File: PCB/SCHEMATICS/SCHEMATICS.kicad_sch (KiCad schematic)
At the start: 0 parts

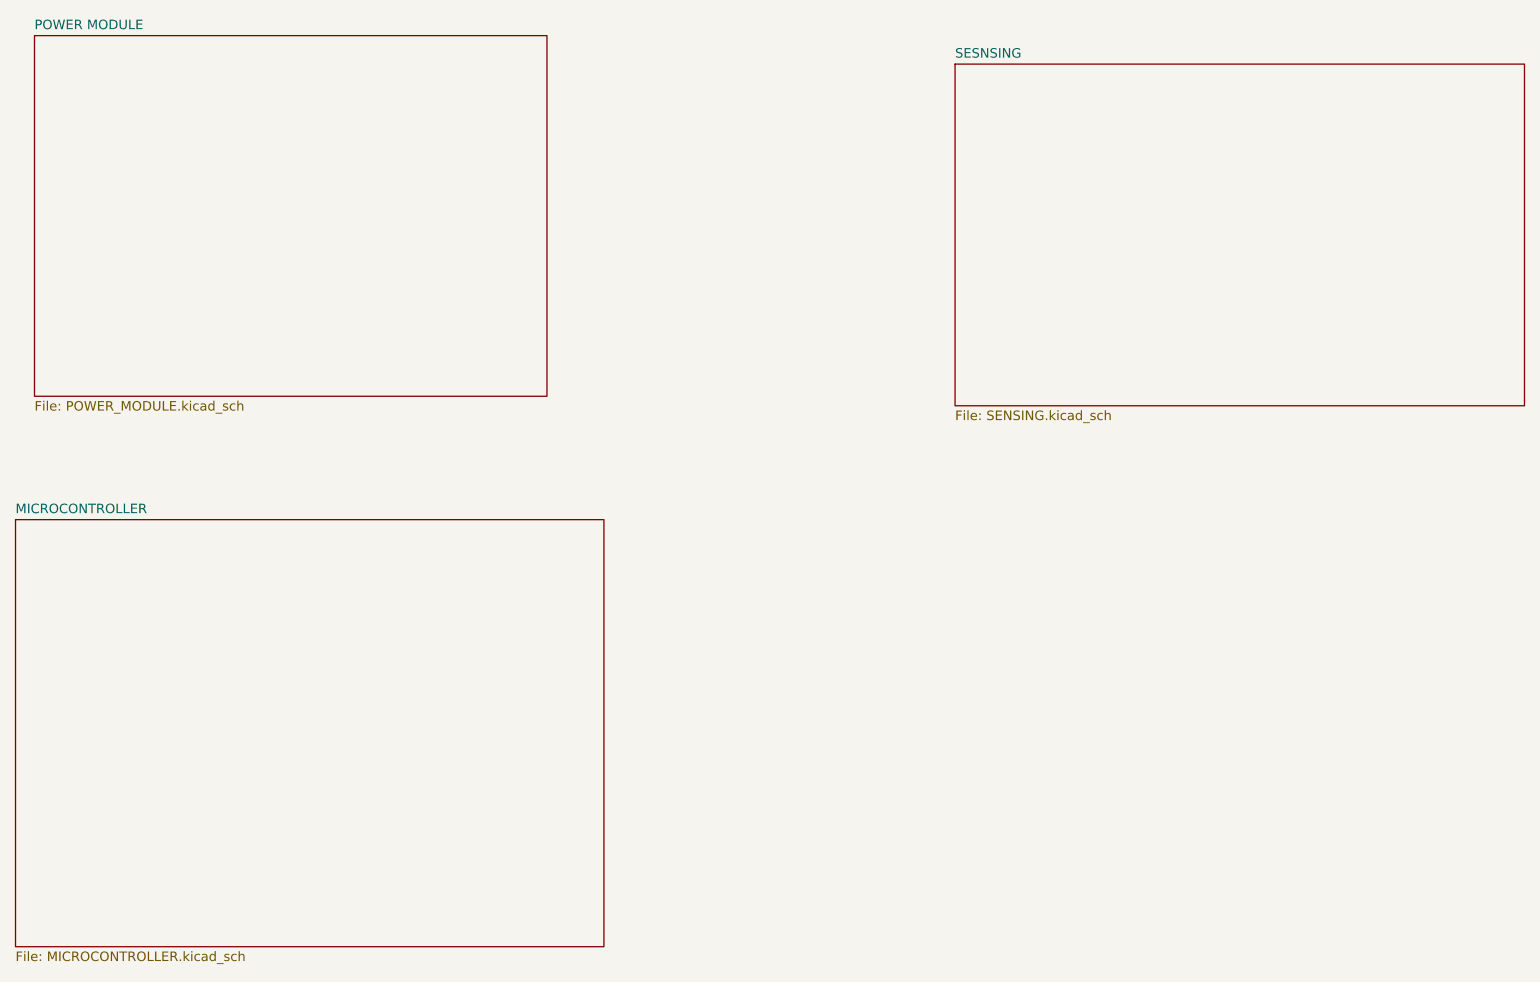
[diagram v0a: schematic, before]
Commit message: Fixed ercs
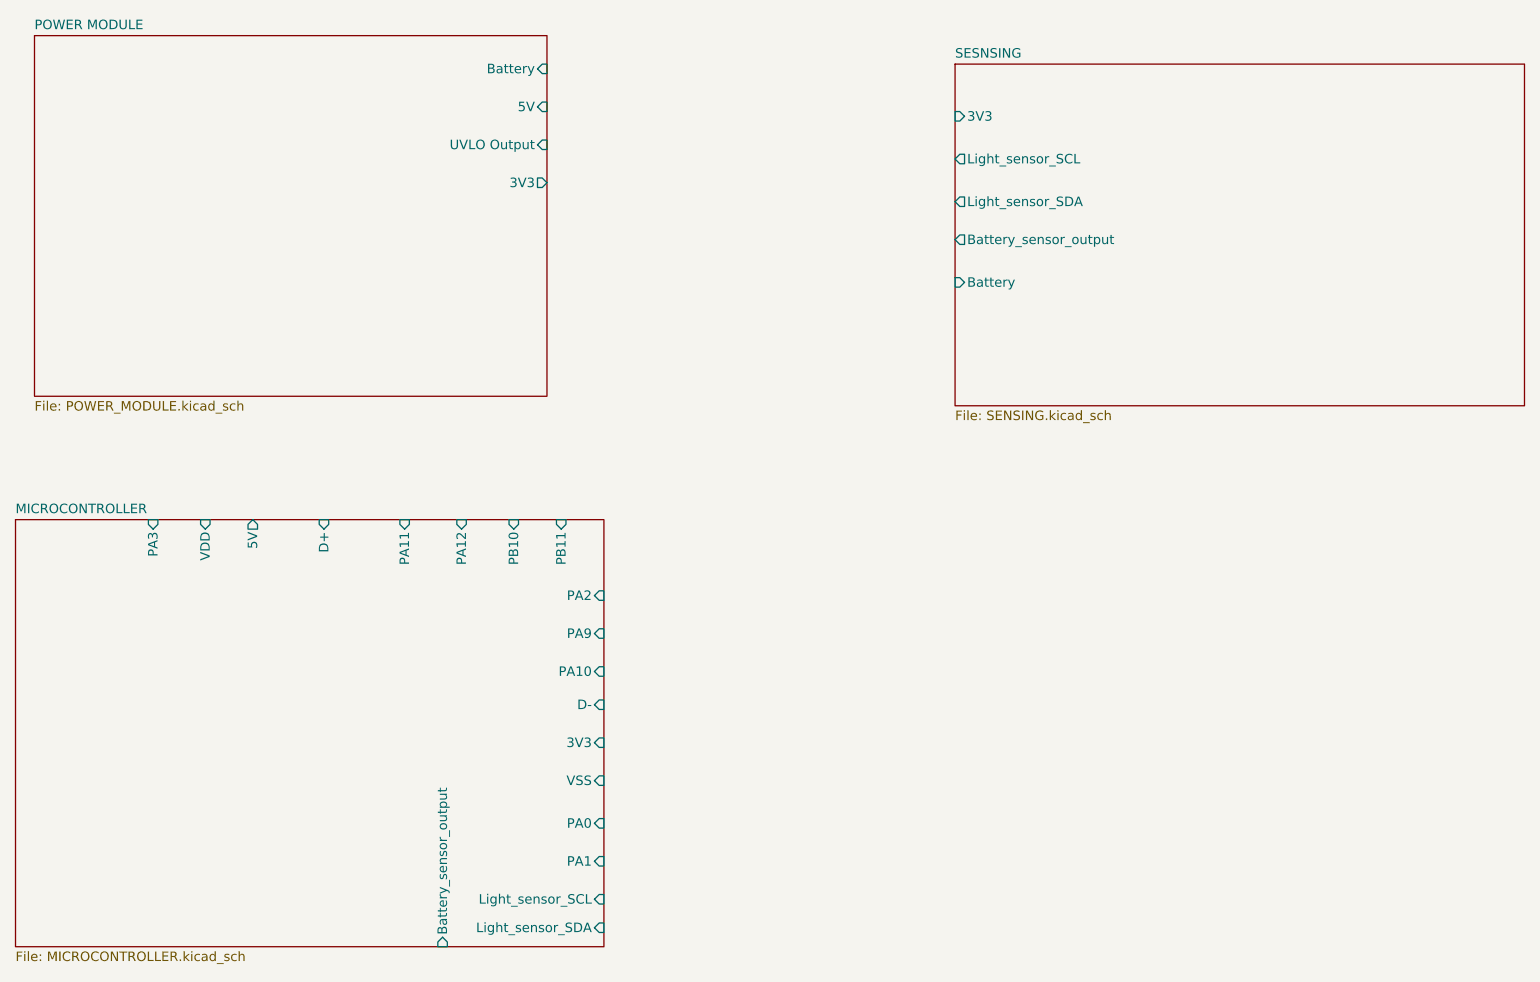
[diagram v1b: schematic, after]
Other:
- sheet MICROCONTROLLER ports: added 3V3, 5V, Battery_sensor_output, D+, D-, Light_sensor_SCL, Light_sensor_SDA, PA0, PA1, PA10, PA11, PA12, PA2, PA3, PA9, PB10, PB11, VDD, VSS; removed none
- sheet POWER MODULE ports: added 3V3, 5V, Battery, UVLO Output; removed none
- sheet SESNSING ports: added 3V3, Battery, Battery_sensor_output, Light_sensor_SCL, Light_sensor_SDA; removed none
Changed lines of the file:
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@@
       (effects (font (size 1.27 1.27)) (justify left top))
+    )
+    (pin "3V3" input (at 171.45 46.355 180)
+      (effects (font (size 1.27 1.27)) (justify left))
+    )
+    (pin "Light_sensor_SCL" output (at 171.45 52.07 180)
+      (effects (font (size 1.27 1.27)) (justify left))
+    )
+    (pin "Light_sensor_SDA" output (at 171.45 57.785 180)
+      (effects (font (size 1.27 1.27)) (justify left))
+    )
+    (pin "Battery_sensor_output" output (at 171.45 62.865 180)
+      (effects (font (size 1.27 1.27)) (justify left))
+    )
+    (pin "Battery" input (at 171.45 68.58 180)
+      (effects (font (size 1.27 1.27)) (justify left))
     )
     (instances
@@
       (effects (font (size 1.27 1.27)) (justify left top))
     )
+    (pin "Battery" input (at 116.84 40.005 0)
+      (effects (font (size 1.27 1.27)) (justify right))
+    )
+    (pin "5V" input (at 116.84 45.085 0)
+      (effects (font (size 1.27 1.27)) (justify right))
+    )
+    (pin "UVLO Output" input (at 116.84 50.165 0)
+      (effects (font (size 1.27 1.27)) (justify right))
+    )
+    (pin "3V3" output (at 116.84 55.245 0)
+      (effects (font (size 1.27 1.27)) (justify right))
+    )
     (instances
       (project "SCHEMATICS"
@@
       (effects (font (size 1.27 1.27)) (justify left top))
     )
+    (pin "D+" input (at 86.995 100.33 90)
+      (effects (font (size 1.27 1.27)) (justify right))
+    )
+    (pin "PA11" input (at 97.79 100.33 90)
+      (effects (font (size 1.27 1.27)) (justify right))
+    )
+    (pin "PA12" input (at 105.41 100.33 90)
+      (effects (font (size 1.27 1.27)) (justify right))
+    )
+    (pin "PB10" input (at 112.395 100.33 90)
+      (effects (font (size 1.27 1.27)) (justify right))
+    )
+    (pin "PB11" input (at 118.745 100.33 90)
+      (effects (font (size 1.27 1.27)) (justify right))
+    )
+    (pin "5V" output (at 77.47 100.33 90)
+      (effects (font (size 1.27 1.27)) (justify right))
+    )
+    (pin "VDD" input (at 71.12 100.33 90)
+      (effects (font (size 1.27 1.27)) (justify right))
+    )
+    (pin "PA3" input (at 64.135 100.33 90)
+      (effects (font (size 1.27 1.27)) (justify right))
+    )
+    (pin "PA2" input (at 124.46 110.49 0)
+      (effects (font (size 1.27 1.27)) (justify right))
+    )
+    (pin "PA9" input (at 124.46 115.57 0)
+      (effects (font (size 1.27 1.27)) (justify right))
+    )
+    (pin "PA10" input (at 124.46 120.65 0)
+      (effects (font (size 1.27 1.27)) (justify right))
+    )
+    (pin "D-" input (at 124.46 125.095 0)
+      (effects (font (size 1.27 1.27)) (justify right))
+    )
+    (pin "3V3" input (at 124.46 130.175 0)
+      (effects (font (size 1.27 1.27)) (justify right))
+    )
+    (pin "VSS" input (at 124.46 135.255 0)
+      (effects (font (size 1.27 1.27)) (justify right))
+    )
+    (pin "PA0" input (at 124.46 140.97 0)
+      (effects (font (size 1.27 1.27)) (justify right))
+    )
+    (pin "PA1" input (at 124.46 146.05 0)
+      (effects (font (size 1.27 1.27)) (justify right))
+    )
+    (pin "Light_sensor_SCL" input (at 124.46 151.13 0)
+      (effects (font (size 1.27 1.27)) (justify right))
+    )
+    (pin "Light_sensor_SDA" input (at 124.46 154.94 0)
+      (effects (font (size 1.27 1.27)) (justify right))
+    )
+    (pin "Battery_sensor_output" input (at 102.87 157.48 270)
+      (effects (font (size 1.27 1.27)) (justify left))
+    )
     (instances

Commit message: Fixing ERCs
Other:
- sheet MICROCONTROLLER ports: added none; removed D+, D-, PA0, PA1, PA10, PA11, PA12, PA2, PA3, PA9, PB10, PB11, VDD, VSS
- sheet POWER MODULE ports: added none; removed UVLO Output
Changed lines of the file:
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@@
 (kicad_sch (version 20230121) (generator eeschema)
   (paper "A4")
-  (sheet (at 171.45 39.37) (size 76.2 45.72) (fields_autoplaced)
+  (junction (at 121.92 42.545) (diameter 0) (color 0 0 0 0)
+  )
+  (wire (pts (xy 146.05 114.935) (xy 146.05 54.61))
+    (stroke (width 0) (type default))
+  )
+  (wire (pts (xy 144.78 111.125) (xy 144.78 48.895))
+    (stroke (width 0) (type default))
+  )
+  (wire (pts (xy 124.46 111.125) (xy 144.78 111.125))
+    (stroke (width 0) (type default))
+  )
+  (wire (pts (xy 121.92 42.545) (xy 170.18 42.545))
+    (stroke (width 0) (type default))
+  )
+  (wire (pts (xy 124.46 114.935) (xy 146.05 114.935))
+    (stroke (width 0) (type default))
+  )
+  (wire (pts (xy 112.395 83.82) (xy 112.395 100.33))
+    (stroke (width 0) (type default))
+  )
+  (wire (pts (xy 121.92 100.33) (xy 121.92 42.545))
+    (stroke (width 0) (type default))
+  )
+  (wire (pts (xy 116.84 42.545) (xy 121.92 42.545))
+    (stroke (width 0) (type default))
+  )
+  (wire (pts (xy 116.84 40.005) (xy 170.18 40.005))
+    (stroke (width 0) (type default))
+  )
+  (wire (pts (xy 146.685 59.69) (xy 170.18 59.69))
+    (stroke (width 0) (type default))
+  )
+  (wire (pts (xy 124.46 118.745) (xy 146.685 118.745))
+    (stroke (width 0) (type default))
+  )
+  (wire (pts (xy 146.05 54.61) (xy 170.18 54.61))
+    (stroke (width 0) (type default))
+  )
+  (wire (pts (xy 144.78 48.895) (xy 170.18 48.895))
+    (stroke (width 0) (type default))
+  )
+  (wire (pts (xy 146.685 118.745) (xy 146.685 59.69))
+    (stroke (width 0) (type default))
+  )
+  (sheet (at 170.18 36.195) (size 76.2 45.72) (fields_autoplaced)
     (stroke (width 0.1524) (type solid))
     (fill (color 0 0 0 0.0000))
-    (property "Sheetname" "SESNSING" (at 171.45 38.6584 0)
+    (property "Sheetname" "SESNSING" (at 170.18 35.4834 0)
       (effects (font (size 1.27 1.27)) (justify left bottom))
     )
-    (property "Sheetfile" "SENSING.kicad_sch" (at 171.45 85.6746 0)
+    (property "Sheetfile" "SENSING.kicad_sch" (at 170.18 82.4996 0)
       (effects (font (size 1.27 1.27)) (justify left top))
     )
-    (pin "3V3" input (at 171.45 46.355 180)
+    (pin "3V3" input (at 170.18 42.545 180)
       (effects (font (size 1.27 1.27)) (justify left))
     )
-    (pin "Light_sensor_SCL" output (at 171.45 52.07 180)
+    (pin "Light_sensor_SCL" output (at 170.18 48.895 180)
       (effects (font (size 1.27 1.27)) (justify left))
     )
-    (pin "Light_sensor_SDA" output (at 171.45 57.785 180)
+    (pin "Light_sensor_SDA" output (at 170.18 54.61 180)
       (effects (font (size 1.27 1.27)) (justify left))
     )
-    (pin "Battery_sensor_output" output (at 171.45 62.865 180)
+    (pin "Battery_sensor_output" output (at 170.18 59.69 180)
       (effects (font (size 1.27 1.27)) (justify left))
     )
-    (pin "Battery" input (at 171.45 68.58 180)
+    (pin "Battery" input (at 170.18 40.005 180)
       (effects (font (size 1.27 1.27)) (justify left))
     )
@@
       (effects (font (size 1.27 1.27)) (justify right))
     )
-    (pin "5V" input (at 116.84 45.085 0)
-      (effects (font (size 1.27 1.27)) (justify right))
+    (pin "5V" input (at 112.395 83.82 270)
+      (effects (font (size 1.27 1.27)) (justify left))
     )
-    (pin "UVLO Output" input (at 116.84 50.165 0)
-      (effects (font (size 1.27 1.27)) (justify right))
-    )
-    (pin "3V3" output (at 116.84 55.245 0)
+    (pin "3V3" output (at 116.84 42.545 0)
       (effects (font (size 1.27 1.27)) (justify right))
     )
@@
       (effects (font (size 1.27 1.27)) (justify left top))
     )
-    (pin "D+" input (at 86.995 100.33 90)
+    (pin "5V" output (at 112.395 100.33 90)
       (effects (font (size 1.27 1.27)) (justify right))
     )
-    (pin "PA11" input (at 97.79 100.33 90)
+    (pin "3V3" input (at 121.92 100.33 90)
       (effects (font (size 1.27 1.27)) (justify right))
     )
-    (pin "PA12" input (at 105.41 100.33 90)
+    (pin "Battery_sensor_output" input (at 124.46 118.745 0)
       (effects (font (size 1.27 1.27)) (justify right))
     )
-    (pin "PB10" input (at 112.395 100.33 90)
+    (pin "Light_sensor_SDA" input (at 124.46 114.935 0)
       (effects (font (size 1.27 1.27)) (justify right))
     )
-    (pin "PB11" input (at 118.745 100.33 90)
+    (pin "Light_sensor_SCL" input (at 124.46 111.125 0)
       (effects (font (size 1.27 1.27)) (justify right))
     )
-    (pin "5V" output (at 77.47 100.33 90)
-      (effects (font (size 1.27 1.27)) (justify right))
-    )
-    (pin "VDD" input (at 71.12 100.33 90)
-      (effects (font (size 1.27 1.27)) (justify right))
-    )
-    (pin "PA3" input (at 64.135 100.33 90)
-      (effects (font (size 1.27 1.27)) (justify right))
-    )
-    (pin "PA2" input (at 124.46 110.49 0)
-      (effects (font (size 1.27 1.27)) (justify right))
-    )
-    (pin "PA9" input (at 124.46 115.57 0)
-      (effects (font (size 1.27 1.27)) (justify right))
-    )
-    (pin "PA10" input (at 124.46 120.65 0)
-      (effects (font (size 1.27 1.27)) (justify right))
-    )
-    (pin "D-" input (at 124.46 125.095 0)
-      (effects (font (size 1.27 1.27)) (justify right))
-    )
-    (pin "3V3" input (at 124.46 130.175 0)
-      (effects (font (size 1.27 1.27)) (justify right))
-    )
-    (pin "VSS" input (at 124.46 135.255 0)
-      (effects (font (size 1.27 1.27)) (justify right))
-    )
-    (pin "PA0" input (at 124.46 140.97 0)
-      (effects (font (size 1.27 1.27)) (justify right))
-    )
-    (pin "PA1" input (at 124.46 146.05 0)
-      (effects (font (size 1.27 1.27)) (justify right))
-    )
-    (pin "Light_sensor_SCL" input (at 124.46 151.13 0)
-      (effects (font (size 1.27 1.27)) (justify right))
-    )
-    (pin "Light_sensor_SDA" input (at 124.46 154.94 0)
-      (effects (font (size 1.27 1.27)) (justify right))
-    )
-    (pin "Battery_sensor_output" input (at 102.87 157.48 270)
-      (effects (font (size 1.27 1.27)) (justify left))
-    )
     (instances
